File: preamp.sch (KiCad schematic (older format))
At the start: 44 parts, among them P1 CONN_01X04, P2 CONN_01X02, P3 CONN_01X04, P4 CONN_01X01, T1 TRANSFO2, U1 OPA137N, U2 LM7815CT, U3 LM7915CT, U4 OPA137N

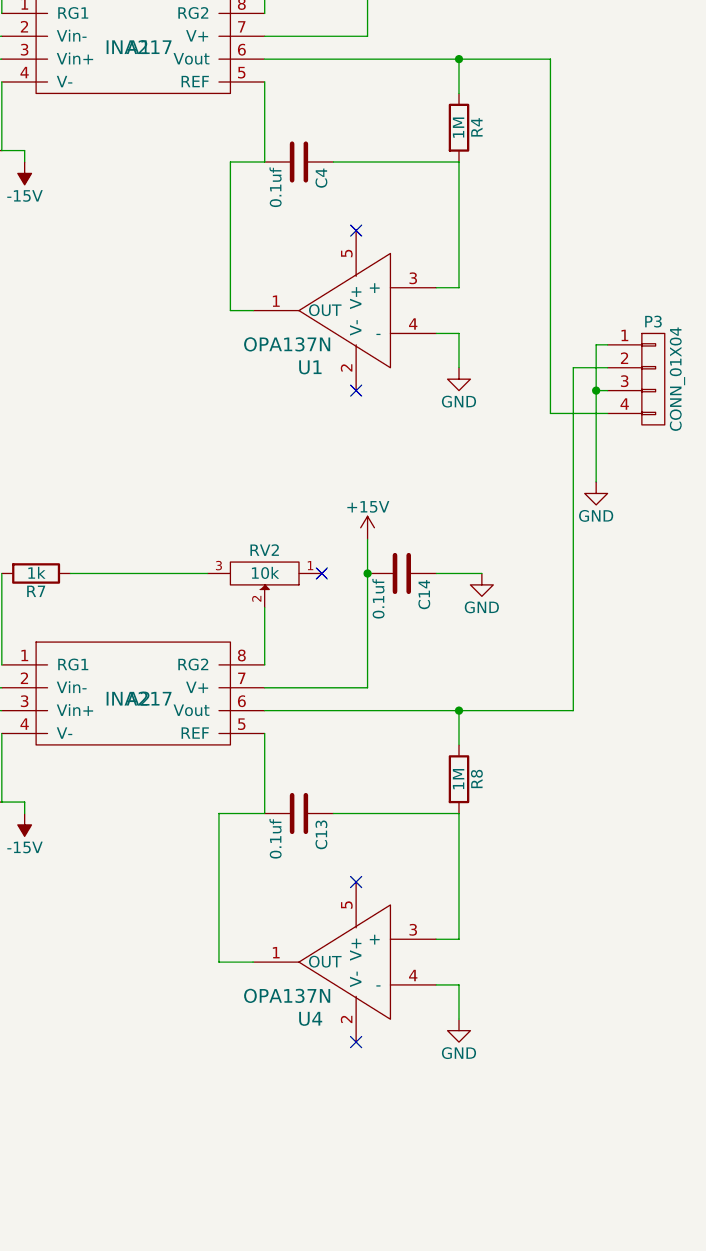
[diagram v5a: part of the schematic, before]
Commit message: Fix transformer value to adjust for RMS vs peak to peak voltage.  Add extra filtering caps at PSU output.  Fix the diode bridge pads.
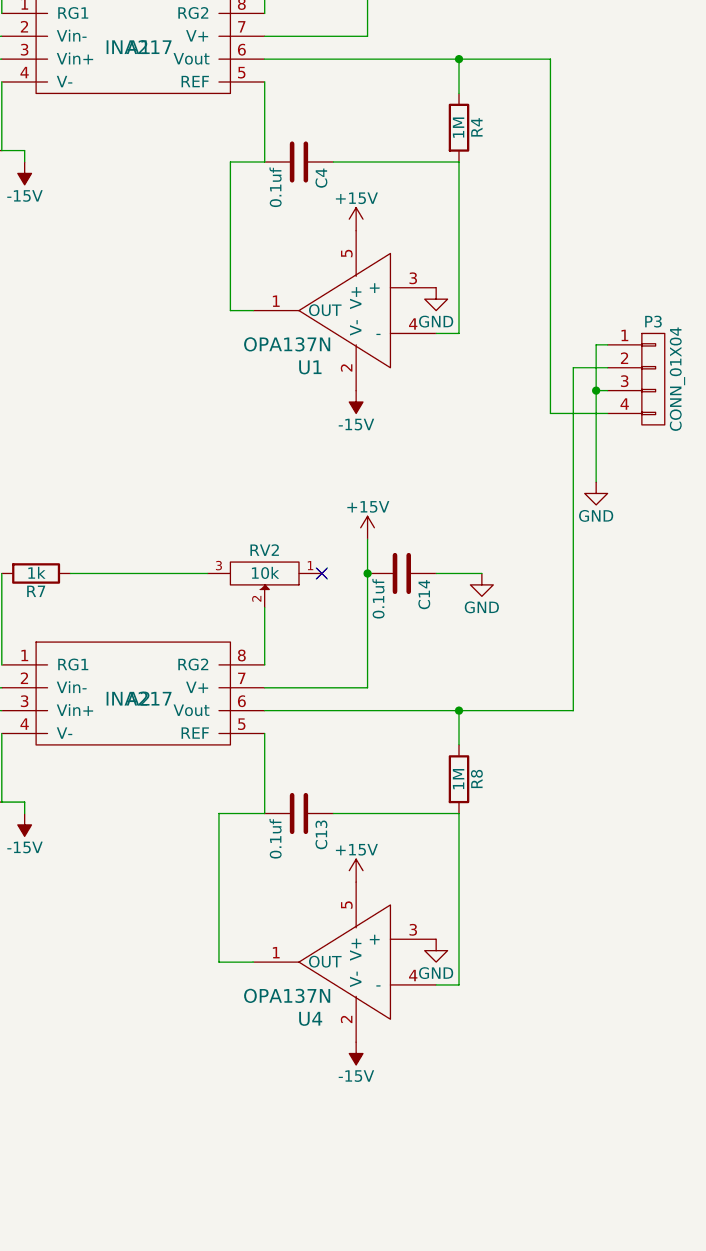
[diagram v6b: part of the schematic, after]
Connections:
- net +15V: now also U1.5 (V+), U4.5 (V+)
- net -15V: now also U1.2 (V-), U4.2 (V-)
- net GND: now also U1.3 (+), U4.3 (+); no longer U1.4 (-), U4.4 (-)
- net at C4.1, R4.2: now also U1.4 (-); no longer U1.3 (+)
- net at C13.1, R8.2: now also U4.4 (-); no longer U4.3 (+)
- no-connect marks 6 -> 2
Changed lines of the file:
@@
 L GND #PWR06
 U 1 1 55749DC2
-P 10050 3000
-F 0 "#PWR06" H 10050 2750 50  0001 C CNN
-F 1 "GND" H 10050 2850 50  0000 C CNN
-F 2 "" H 10050 3000 60  0000 C CNN
-F 3 "" H 10050 3000 60  0000 C CNN
-	1    10050 3000
+P 9950 2650
+F 0 "#PWR06" H 9950 2400 50  0001 C CNN
+F 1 "GND" H 9950 2500 50  0000 C CNN
+F 2 "" H 9950 2650 60  0000 C CNN
+F 3 "" H 9950 2650 60  0000 C CNN
+	1    9950 2650
 	1    0    0    -1
 $EndComp
@@
 L GND #PWR013
 U 1 1 557A9BC4
-P 10050 5850
-F 0 "#PWR013" H 10050 5600 50  0001 C CNN
-F 1 "GND" H 10050 5700 50  0000 C CNN
-F 2 "" H 10050 5850 60  0000 C CNN
-F 3 "" H 10050 5850 60  0000 C CNN
-	1    10050 5850
+P 9950 5500
+F 0 "#PWR013" H 9950 5250 50  0001 C CNN
+F 1 "GND" H 9950 5350 50  0000 C CNN
+F 2 "" H 9950 5500 60  0000 C CNN
+F 3 "" H 9950 5500 60  0000 C CNN
+	1    9950 5500
 	1    0    0    -1
 $EndComp
@@
 	1    0    0    -1
 $EndComp
-NoConn ~ 9600 2400
-NoConn ~ 9600 3100
+$Comp
+L GND #PWR026
+U 1 1 557E5A9A
+P 4900 5450
+F 0 "#PWR026" H 4900 5200 50  0001 C CNN
+F 1 "GND" H 4900 5300 50  0000 C CNN
+F 2 "" H 4900 5450 60  0000 C CNN
+F 3 "" H 4900 5450 60  0000 C CNN
+	1    4900 5450
+	1    0    0    -1
+$EndComp
+$Comp
+L GND #PWR027
+U 1 1 557E632B
+P 7250 2350
+F 0 "#PWR027" H 7250 2100 50  0001 C CNN
+F 1 "GND" H 7250 2200 50  0000 C CNN
+F 2 "" H 7250 2350 60  0000 C CNN
+F 3 "" H 7250 2350 60  0000 C CNN
+	1    7250 2350
+	1    0    0    -1
+$EndComp
+$Comp
+L GND #PWR028
+U 1 1 557E6C53
+P 4050 7150
+F 0 "#PWR028" H 4050 6900 50  0001 C CNN
+F 1 "GND" H 4050 7000 50  0000 C CNN
+F 2 "" H 4050 7150 60  0000 C CNN
+F 3 "" H 4050 7150 60  0000 C CNN
+	1    4050 7150
+	1    0    0    -1
+$EndComp
+$Comp
+L GND #PWR029
+U 1 1 557E7348
+P 2000 4550
+F 0 "#PWR029" H 2000 4300 50  0001 C CNN
+F 1 "GND" H 2000 4400 50  0000 C CNN
+F 2 "" H 2000 4550 60  0000 C CNN
+F 3 "" H 2000 4550 60  0000 C CNN
+	1    2000 4550
+	1    0    0    -1
+$EndComp
+$Comp
+L PWR_FLAG #FLG030
+U 1 1 557E7388
+P 2000 4300
+F 0 "#FLG030" H 2000 4395 50  0001 C CNN
+F 1 "PWR_FLAG" H 2000 4480 50  0000 C CNN
+F 2 "" H 2000 4300 60  0000 C CNN
+F 3 "" H 2000 4300 60  0000 C CNN
+	1    2000 4300
+	1    0    0    -1
+$EndComp
+$Comp
+L CONN_01X01 P4
+U 1 1 558063EE
+P 2100 5150
+F 0 "P4" H 2100 5250 50  0000 C CNN
+F 1 "CONN_01X01" V 2200 5150 50  0000 C CNN
+F 2 "Pin_Headers:Pin_Header_Straight_1x01" H 2100 5150 60  0001 C CNN
+F 3 "" H 2100 5150 60  0000 C CNN
+	1    2100 5150
+	-1   0    0    1
+$EndComp
+$Comp
+L GND #PWR031
+U 1 1 558082FD
+P 2500 5950
+F 0 "#PWR031" H 2500 5700 50  0001 C CNN
+F 1 "GND" H 2500 5800 50  0000 C CNN
+F 2 "" H 2500 5950 60  0000 C CNN
+F 3 "" H 2500 5950 60  0000 C CNN
+	1    2500 5950
+	1    0    0    -1
+$EndComp
 $Comp
 L OPA137N U4
@@
 	1    0    0    -1
 $EndComp
-NoConn ~ 9600 5250
-NoConn ~ 9600 5950
-$Comp
-L GND #PWR026
-U 1 1 557E5A9A
-P 4900 5450
-F 0 "#PWR026" H 4900 5200 50  0001 C CNN
-F 1 "GND" H 4900 5300 50  0000 C CNN
-F 2 "" H 4900 5450 60  0000 C CNN
-F 3 "" H 4900 5450 60  0000 C CNN
-	1    4900 5450
-	1    0    0    -1
-$EndComp
-$Comp
-L GND #PWR027
-U 1 1 557E632B
-P 7250 2350
-F 0 "#PWR027" H 7250 2100 50  0001 C CNN
-F 1 "GND" H 7250 2200 50  0000 C CNN
-F 2 "" H 7250 2350 60  0000 C CNN
-F 3 "" H 7250 2350 60  0000 C CNN
-	1    7250 2350
-	1    0    0    -1
-$EndComp
-$Comp
-L GND #PWR028
-U 1 1 557E6C53
-P 4050 7150
-F 0 "#PWR028" H 4050 6900 50  0001 C CNN
-F 1 "GND" H 4050 7000 50  0000 C CNN
-F 2 "" H 4050 7150 60  0000 C CNN
-F 3 "" H 4050 7150 60  0000 C CNN
-	1    4050 7150
-	1    0    0    -1
-$EndComp
-$Comp
-L GND #PWR029
-U 1 1 557E7348
-P 2000 4550
-F 0 "#PWR029" H 2000 4300 50  0001 C CNN
-F 1 "GND" H 2000 4400 50  0000 C CNN
-F 2 "" H 2000 4550 60  0000 C CNN
-F 3 "" H 2000 4550 60  0000 C CNN
-	1    2000 4550
-	1    0    0    -1
-$EndComp
-$Comp
-L PWR_FLAG #FLG030
-U 1 1 557E7388
-P 2000 4300
-F 0 "#FLG030" H 2000 4395 50  0001 C CNN
-F 1 "PWR_FLAG" H 2000 4480 50  0000 C CNN
-F 2 "" H 2000 4300 60  0000 C CNN
-F 3 "" H 2000 4300 60  0000 C CNN
-	1    2000 4300
-	1    0    0    -1
-$EndComp
 Wire Wire Line
 	9200 1200 9200 1450
@@
 	9050 2750 9150 2750
 Wire Wire Line
-	9950 2850 10050 2850
-Wire Wire Line
-	10050 2850 10050 3000
-Wire Wire Line
-	9950 2650 10050 2650
-Wire Wire Line
-	10050 2650 10050 2100
+	10050 2100 10050 2850
 Wire Wire Line
 	9000 4950 9000 5600
@@
 	9000 5600 9150 5600
 Wire Wire Line
-	9950 5500 10050 5500
-Wire Wire Line
-	10050 5500 10050 4950
-Wire Wire Line
-	9950 5700 10050 5700
-Wire Wire Line
-	10050 5700 10050 5850
+	10050 4950 10050 5700
 Wire Wire Line
 	5700 4000 5700 2800
@@
 Wire Wire Line
 	2000 4300 2000 4550
-$Comp
-L CONN_01X01 P4
-U 1 1 558063EE
-P 2100 5150
-F 0 "P4" H 2100 5250 50  0000 C CNN
-F 1 "CONN_01X01" V 2200 5150 50  0000 C CNN
-F 2 "Pin_Headers:Pin_Header_Straight_1x01" H 2100 5150 60  0001 C CNN
-F 3 "" H 2100 5150 60  0000 C CNN
-	1    2100 5150
-	-1   0    0    1
-$EndComp
 Wire Wire Line
 	2350 6350 4000 6350
@@
 Wire Wire Line
 	3300 6250 3300 6850
-$Comp
-L GND #PWR031
-U 1 1 558082FD
-P 2500 5950
-F 0 "#PWR031" H 2500 5700 50  0001 C CNN
-F 1 "GND" H 2500 5800 50  0000 C CNN
-F 2 "" H 2500 5950 60  0000 C CNN
-F 3 "" H 2500 5950 60  0000 C CNN
-	1    2500 5950
-	1    0    0    -1
-$EndComp
 Wire Wire Line
 	2350 5950 2500 5950
@@
 Wire Wire Line
 	3300 4850 4250 4850
+Wire Wire Line
+	10050 5700 9950 5700
+Wire Wire Line
+	10050 2850 9950 2850
+$Comp
+L -15V #PWR?
+U 1 1 5585D9AC
+P 9600 5950
+F 0 "#PWR?" H 9600 6050 50  0001 C CNN
+F 1 "-15V" H 9600 6100 50  0000 C CNN
+F 2 "" H 9600 5950 60  0000 C CNN
+F 3 "" H 9600 5950 60  0000 C CNN
+	1    9600 5950
+	-1   0    0    1
+$EndComp
+$Comp
+L +15V #PWR?
+U 1 1 5585D9EC
+P 9600 5250
+F 0 "#PWR?" H 9600 5100 50  0001 C CNN
+F 1 "+15V" H 9600 5390 50  0000 C CNN
+F 2 "" H 9600 5250 60  0000 C CNN
+F 3 "" H 9600 5250 60  0000 C CNN
+	1    9600 5250
+	1    0    0    -1
+$EndComp
+$Comp
+L -15V #PWR?
+U 1 1 5585DA98
+P 9600 3100
+F 0 "#PWR?" H 9600 3200 50  0001 C CNN
+F 1 "-15V" H 9600 3250 50  0000 C CNN
+F 2 "" H 9600 3100 60  0000 C CNN
+F 3 "" H 9600 3100 60  0000 C CNN
+	1    9600 3100
+	-1   0    0    1
+$EndComp
+$Comp
+L +15V #PWR?
+U 1 1 5585DAD8
+P 9600 2400
+F 0 "#PWR?" H 9600 2250 50  0001 C CNN
+F 1 "+15V" H 9600 2540 50  0000 C CNN
+F 2 "" H 9600 2400 60  0000 C CNN
+F 3 "" H 9600 2400 60  0000 C CNN
+	1    9600 2400
+	1    0    0    -1
+$EndComp
 $EndSCHEMATC
